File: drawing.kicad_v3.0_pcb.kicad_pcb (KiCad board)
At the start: 2 copper layers, 93 x 65 mm, 42 parts, among them IC1 DW01A-G, J1 Micro USB Chargeport, J2 Conn_01x03, J3 128x32 I2C OLED, J4 TP4056, J5 MK-12C02, J6 Conn_01x02, Q1 FS8205, U1 HT7333-SOT89, U2 ESP-12E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

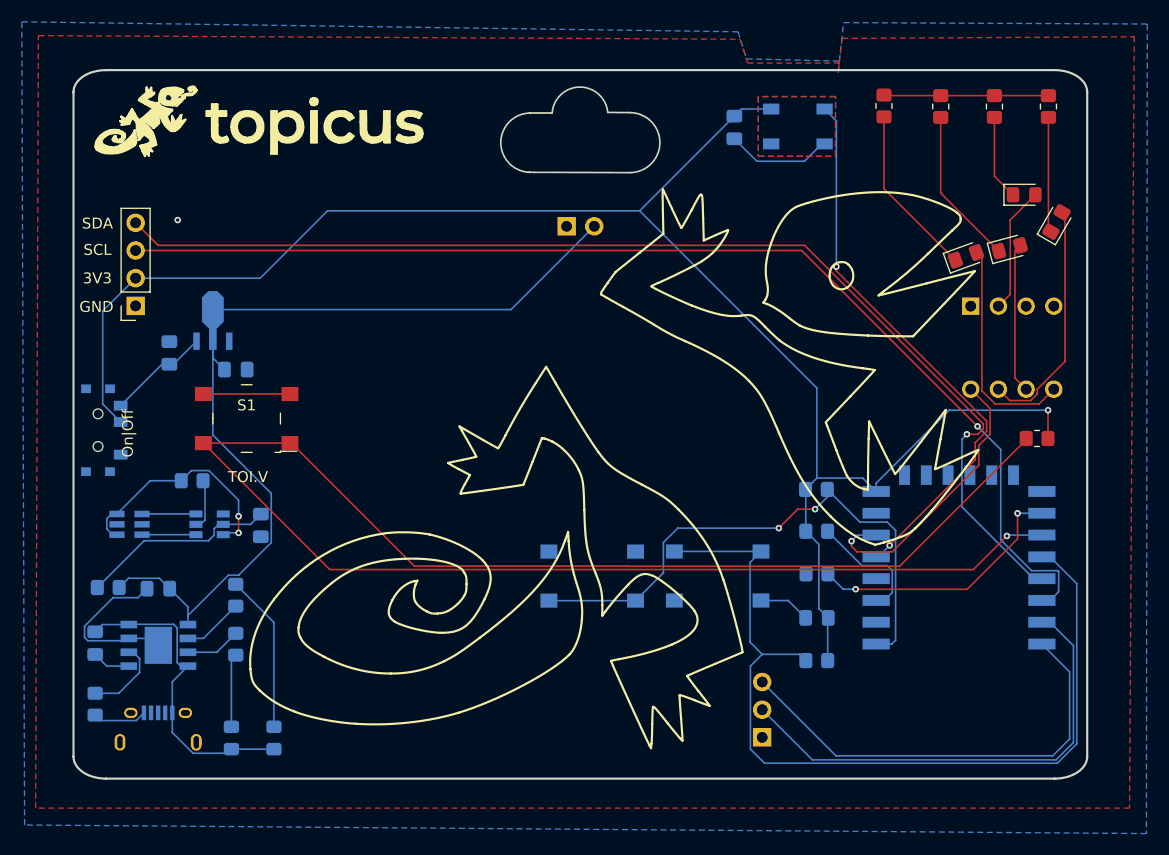
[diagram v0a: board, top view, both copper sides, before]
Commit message: Fixed HT7333 and charging circuit
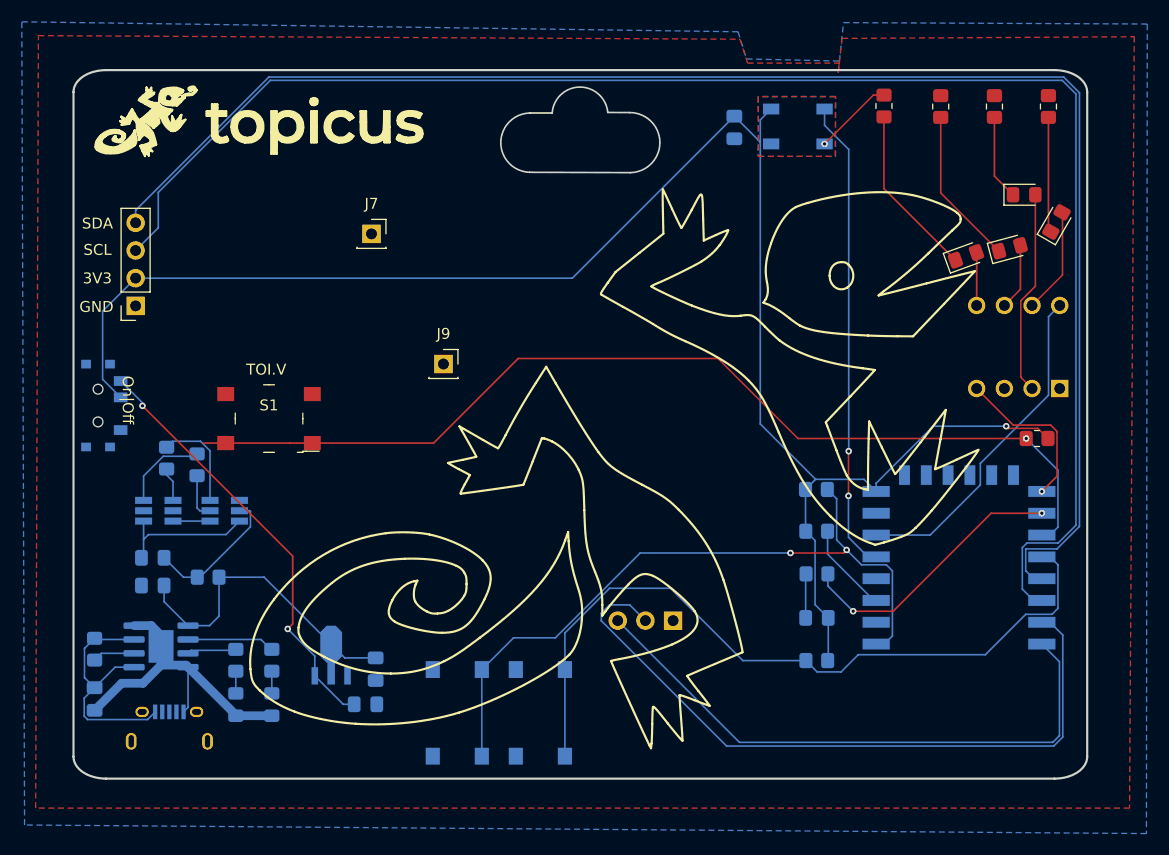
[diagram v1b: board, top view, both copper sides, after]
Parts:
- removed IC1: DW01A-G, user-footprints:SOT95P280X135-6N
- removed J4: TP4056, Custom:SOIC127P600X175-9N
- removed J6: Conn_01x02, Connector_PinSocket_2.54mm:PinSocket_1x02_P2.54mm_Vertical
- removed Q1: FS8205, user-footprints:FS8205
- added J7: Conn_01x01_Female, Connector_PinSocket_2.54mm:PinSocket_1x01_P2.54mm_Vertical, F.Cu at (133.3, 76.5)
- added J9: Conn_01x01_Female, Connector_PinSocket_2.54mm:PinSocket_1x01_P2.54mm_Vertical, F.Cu at (140.0, 88.4)
- added R15: 100, Resistor_SMD:R_0805_2012Metric_Pad1.20x1.40mm_HandSolder, B.Cu at (118.4, 108.0)
- added REF**: OSHW, user-footprints:OSHW, B.Cu at (194.3, 66.0)
- added U4: TP4056, Package_SO:SOIC-8-1EP_3.9x4.9mm_P1.27mm_EP2.29x3mm, B.Cu at (114.0, 114.3)
- added U5: DW01, Package_TO_SOT_SMD:SOT-23-6_Handsoldering, B.Cu at (119.9, 101.9)
- added U6: FS8205A, Package_TO_SOT_SMD:SOT-23-6_Handsoldering, B.Cu at (113.8, 101.9)
- C2: value 100nF / 0.1uF -> 0.1uF
- C4: value 100nF / 0.1uF -> 10uF
- C5: value 10uF -> 0.1uF
- D5: value R-LED -> RED
- D6: value G-LED -> GREEN
- D7: value Neopixel -> Neopixel / SK6812
- R11: value 5k -> 1k
- R12: value 1k -> 10k
- R14: value 100R -> 0R
- moved C6 36.9 mm to (132.8, 119.6), turned to 180 degrees
- moved U1 32.6 mm to (129.7, 115.0)
- moved C7 30.3 mm to (133.7, 116.4), turned to 90 degrees
- moved S3 20.5 mm to (148.8, 120.4), turned to 90 degrees
- moved S2 17.6 mm to (141.2, 120.4), turned to 90 degrees
- moved R11 16.7 mm to (124.2, 115.6)
- moved R12 13.9 mm to (108.0, 114.6)
- moved J2 13.5 mm to (161.0, 111.9), turned to 90 degrees
- moved R14 13.0 mm to (114.6, 97.0), turned to -90 degrees
- moved C4 11.3 mm to (113.3, 108.7), turned to 180 degrees
- moved U3 11.1 mm to (196.5, 90.6), turned to 90 degrees
- moved C2 5.13 mm to (108.0, 119.1)
- moved D5 3.09 mm to (120.9, 119.6)
- moved D6 3.07 mm to (124.2, 119.6)
- moved C5 2.87 mm to (113.3, 106.2)
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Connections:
- net +3V3 renamed 3.3v
- C2 pad 1: GND -> VIN
- C2 pad 2: Net-(C2-Pad2) -> GND
- C4 pad 1: Net-(C4-Pad1) -> BAT+
- C5 pad 1: /Batt+ -> Net-(C5-Pad1)
- C5 pad 2: GND -> BAT-
- C7 pad 2: /Batt+ -> BAT+
- D5 pad 2: Net-(C2-Pad2) -> VIN
- D6 pad 2: Net-(C2-Pad2) -> VIN
- J1 pad 1: Net-(C2-Pad2) -> VIN
- R11 pad 1: GND -> Net-(D6-Pad1)
- R12 pad 2: Net-(D6-Pad1) -> GND
- R13 pad 1: Net-(IC1-Pad2) -> GND
- R13 pad 2: GND -> Net-(R13-Pad2)
- R14 pad 1: /Batt+ -> /OC
- R14 pad 2: Net-(C4-Pad1) -> /G2
- U1 pad 2: /Batt+ -> BAT+
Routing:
- net /Batt+: track 82.1 -> 0.00 mm
- net /BTN: track 168.1 -> 92.9 mm
- net /SCL: track 105.5 -> 146.5 mm, vias 1 -> 0
- net /SDA: track 104.5 -> 142.7 mm, vias 1 -> 0
- net Net-(C6-Pad2): track 9.41 -> 39.5 mm, vias 0 -> 2
- net VIN: track 0.00 -> 29.8 mm
- net Net-(C2-Pad2): track 29.2 -> 0.00 mm
- net BAT+: track 0.00 -> 28.8 mm
- net GND: track 83.2 -> 57.7 mm, vias 3 -> 2
- net /RX: track 43.8 -> 64.9 mm
- net Net-(C4-Pad1): track 18.1 -> 0.00 mm
- net Net-(D1-Pad2): track 20.5 -> 4.87 mm
- net Net-(R6-Pad2): track 51.6 -> 65.0 mm
- net /TX: track 41.4 -> 54.5 mm
- net Net-(C5-Pad1): track 0.00 -> 13.0 mm
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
